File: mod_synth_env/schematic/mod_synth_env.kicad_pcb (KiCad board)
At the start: 2 copper layers, 40.6 x 109.2 mm, 30 parts, among them J1 AudioJack2, J2 AudioJack2, J3 Conn_02x08_Odd_Even, J4 Conn_01x07_Female, J5 Conn_01x07_Male, SW1 SW_Push, SW2 SW_SPDT, U1 TL072

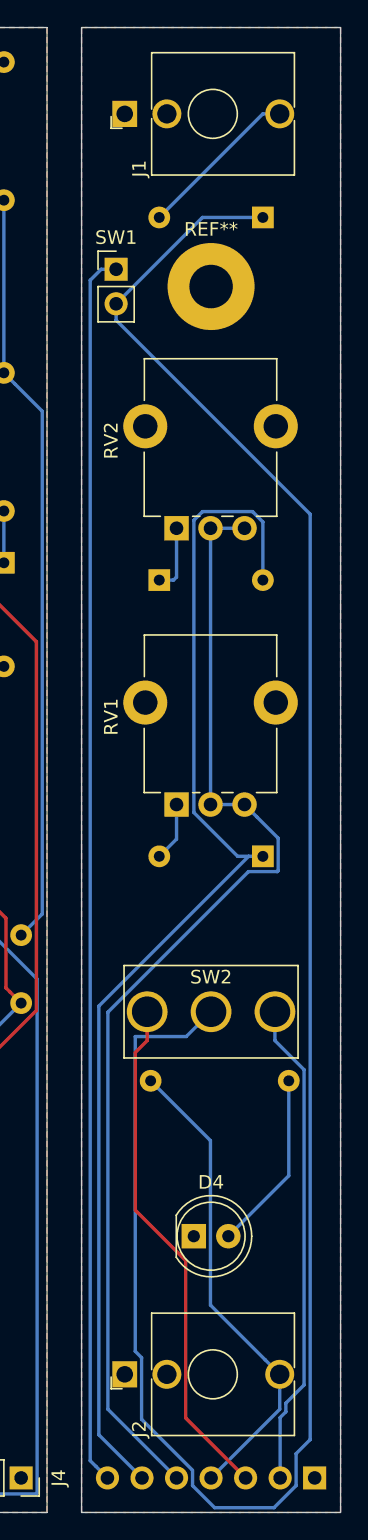
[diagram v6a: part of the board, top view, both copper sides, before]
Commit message: Recreate tracks near switch
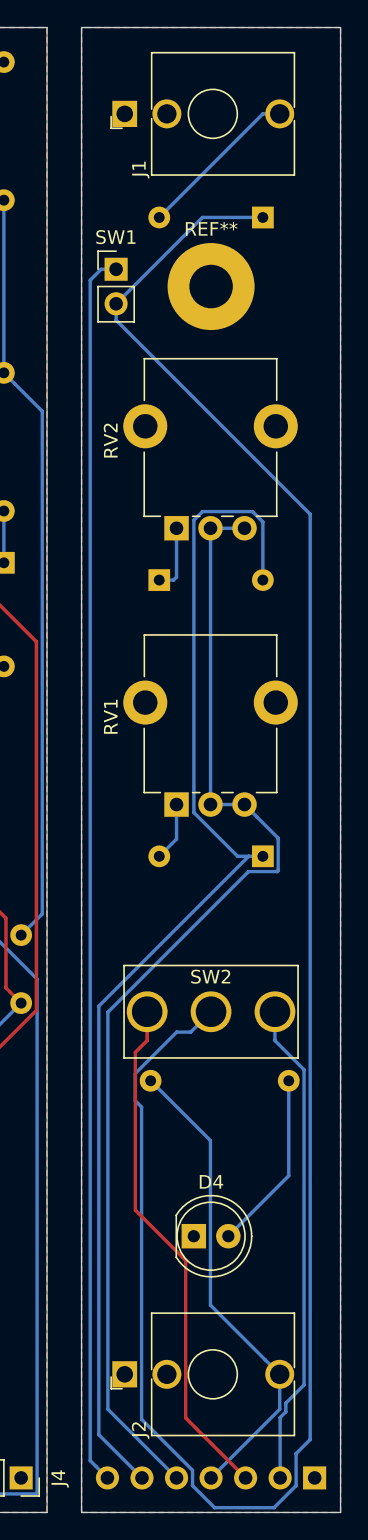
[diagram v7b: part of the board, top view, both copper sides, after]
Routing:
- net Net-(D3-Pad1): track 156.8 -> 155.2 mm
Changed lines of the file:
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@@
     (thickness 1.6)
     (drawings 8)
-    (tracks 158)
+    (tracks 159)
     (zones 0)
     (modules 30)
@@
   (segment (start 73.025 31.75) (end 74.265 31.75) (width 0.25) (layer B.Cu) (net 7))
   (segment (start 65.405 39.37) (end 73.025 31.75) (width 0.25) (layer B.Cu) (net 7))
-  (segment (start 62.23 46.922081) (end 62.23 45.72) (width 0.25) (layer B.Cu) (net 8))
-  (segment (start 76.505011 61.197092) (end 62.23 46.922081) (width 0.25) (layer B.Cu) (net 8))
-  (segment (start 76.505011 129.258989) (end 76.505011 61.197092) (width 0.25) (layer B.Cu) (net 8))
-  (segment (start 75.470001 132.644001) (end 75.470001 130.293999) (width 0.25) (layer B.Cu) (net 8))
-  (segment (start 75.470001 130.293999) (end 76.505011 129.258989) (width 0.25) (layer B.Cu) (net 8))
-  (segment (start 73.844012 134.26999) (end 75.470001 132.644001) (width 0.25) (layer B.Cu) (net 8))
-  (segment (start 67.850001 131.515999) (end 67.850001 132.644001) (width 0.25) (layer B.Cu) (net 8))
-  (segment (start 69.47599 134.26999) (end 73.844012 134.26999) (width 0.25) (layer B.Cu) (net 8))
-  (segment (start 67.850001 132.644001) (end 69.47599 134.26999) (width 0.25) (layer B.Cu) (net 8))
-  (segment (start 64.105001 127.770999) (end 67.850001 131.515999) (width 0.25) (layer B.Cu) (net 8))
-  (segment (start 64.105001 123.234999) (end 64.105001 127.770999) (width 0.25) (layer B.Cu) (net 8))
-  (segment (start 63.638999 122.768997) (end 64.105001 123.234999) (width 0.25) (layer B.Cu) (net 8))
-  (segment (start 63.638999 99.615001) (end 63.638999 122.768997) (width 0.25) (layer B.Cu) (net 8))
-  (segment (start 67.389999 99.615001) (end 63.638999 99.615001) (width 0.25) (layer B.Cu) (net 8))
-  (segment (start 69.215 97.79) (end 67.389999 99.615001) (width 0.25) (layer B.Cu) (net 8))
   (segment (start 68.58 39.37) (end 62.23 45.72) (width 0.25) (layer B.Cu) (net 8))
   (segment (start 73.025 39.37) (end 68.58 39.37) (width 0.25) (layer B.Cu) (net 8))
+  (segment (start 63.644999 102.329999) (end 66.684999 99.289999) (width 0.25) (layer B.Cu) (net 8))
+  (segment (start 63.644999 104.344997) (end 63.644999 102.329999) (width 0.25) (layer B.Cu) (net 8))
+  (segment (start 67.850001 131.515999) (end 64.105001 127.770999) (width 0.25) (layer B.Cu) (net 8))
+  (segment (start 67.850001 132.644001) (end 67.850001 131.515999) (width 0.25) (layer B.Cu) (net 8))
+  (segment (start 69.47599 134.26999) (end 67.850001 132.644001) (width 0.25) (layer B.Cu) (net 8))
+  (segment (start 64.105001 127.770999) (end 64.105001 104.804999) (width 0.25) (layer B.Cu) (net 8))
+  (segment (start 73.844012 134.26999) (end 69.47599 134.26999) (width 0.25) (layer B.Cu) (net 8))
+  (segment (start 62.23 45.72) (end 62.23 46.922081) (width 0.25) (layer B.Cu) (net 8))
+  (segment (start 64.105001 104.804999) (end 63.644999 104.344997) (width 0.25) (layer B.Cu) (net 8))
+  (segment (start 62.23 46.922081) (end 76.505011 61.197092) (width 0.25) (layer B.Cu) (net 8))
+  (segment (start 66.684999 99.289999) (end 67.715001 99.289999) (width 0.25) (layer B.Cu) (net 8))
+  (segment (start 76.505011 61.197092) (end 76.505011 129.258989) (width 0.25) (layer B.Cu) (net 8))
+  (segment (start 75.470001 130.293999) (end 75.470001 132.644001) (width 0.25) (layer B.Cu) (net 8))
+  (segment (start 67.715001 99.289999) (end 69.215 97.79) (width 0.25) (layer B.Cu) (net 8))
+  (segment (start 76.505011 129.258989) (end 75.470001 130.293999) (width 0.25) (layer B.Cu) (net 8))
+  (segment (start 75.470001 132.644001) (end 73.844012 134.26999) (width 0.25) (layer B.Cu) (net 8))
   (segment (start 74.93 109.855) (end 74.93 102.87) (width 0.25) (layer B.Cu) (net 9))
   (segment (start 70.485 114.3) (end 74.93 109.855) (width 0.25) (layer B.Cu) (net 9))
@@
   (segment (start 61.13 43.18) (end 60.325 43.985) (width 0.25) (layer B.Cu) (net 34))
   (segment (start 62.23 43.18) (end 61.13 43.18) (width 0.25) (layer B.Cu) (net 34))
-  (zone (net 31) (net_name /GND_PCB_B) (layer B.Cu) (hatch edge 0.508)
-    (connect_pads (clearance 0.508))
-    (min_thickness 0.254)
-    (fill yes (arc_segments 32) (thermal_gap 0.508) (thermal_bridge_width 0.508))
-    (polygon
-      (pts
-        (xy 59.69 134.62) (xy 78.74 134.62) (xy 78.74 25.4) (xy 59.69 25.4)
-      )
-    )
-  )
-  (zone (net 31) (net_name /GND_PCB_B) (layer F.Cu) (hatch edge 0.508)
-    (connect_pads (clearance 0.508))
-    (min_thickness 0.254)
-    (fill yes (arc_segments 32) (thermal_gap 0.508) (thermal_bridge_width 0.508))
-    (polygon
-      (pts
-        (xy 59.69 25.4) (xy 78.74 25.4) (xy 78.74 134.62) (xy 59.69 134.62)
-      )
-    )
-  )
   (zone (net 1) (net_name GND) (layer B.Cu) (hatch edge 0.508)
     (connect_pads (clearance 0.508))
@@
       )
     )
+  )
+  (zone (net 31) (net_name /GND_PCB_B) (layer B.Cu) (hatch edge 0.508)
+    (connect_pads (clearance 0.508))
+    (min_thickness 0.254)
+    (fill yes (arc_segments 32) (thermal_gap 0.508) (thermal_bridge_width 0.508))
+    (polygon
+      (pts
+        (xy 59.69 25.4) (xy 59.69 134.62) (xy 78.74 134.62) (xy 78.74 25.4)
+      )
+    )
+  )
+  (zone (net 31) (net_name /GND_PCB_B) (layer F.Cu) (hatch edge 0.508)
+    (connect_pads (clearance 0.508))
+    (min_thickness 0.254)
+    (fill yes (arc_segments 32) (thermal_gap 0.508) (thermal_bridge_width 0.508))
+    (polygon
+      (pts
+        (xy 59.69 134.62) (xy 78.74 134.62) (xy 78.74 25.4) (xy 59.69 25.4)
+      )
+    )
